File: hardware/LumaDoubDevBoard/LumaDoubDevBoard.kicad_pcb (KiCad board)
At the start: 4 copper layers, 99.5 x 99.5 mm, 188 parts, among them IC1 TPS2116DRLR, IC2 TPS62A01ADRLR, J2 217179-0001, J3 Conn_01x02_Pin, J4 Conn_01x08, J5 Conn_01x06, J6 Conn_01x08, J7 Conn_02x12_Odd_Even, P1 VGA_Male, P2 VGA_Male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

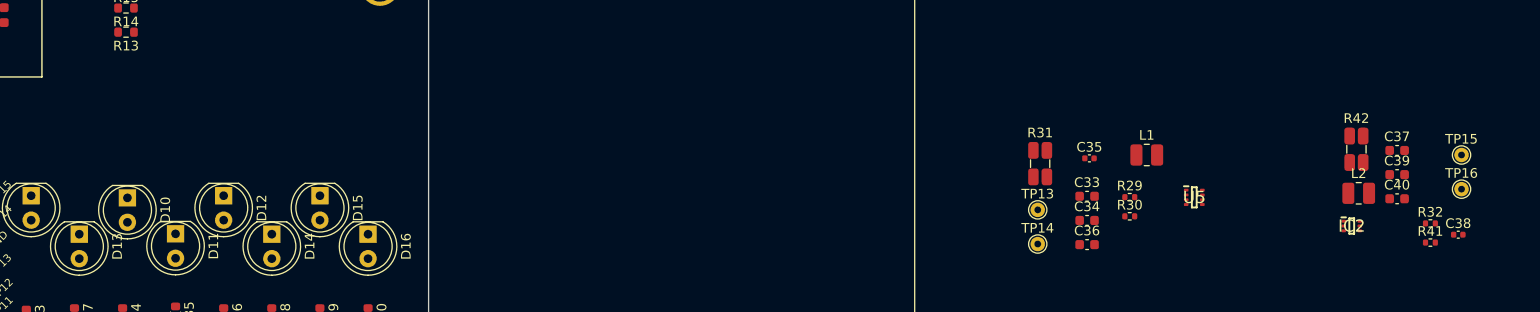
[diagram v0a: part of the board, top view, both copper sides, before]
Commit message: buck converter routing
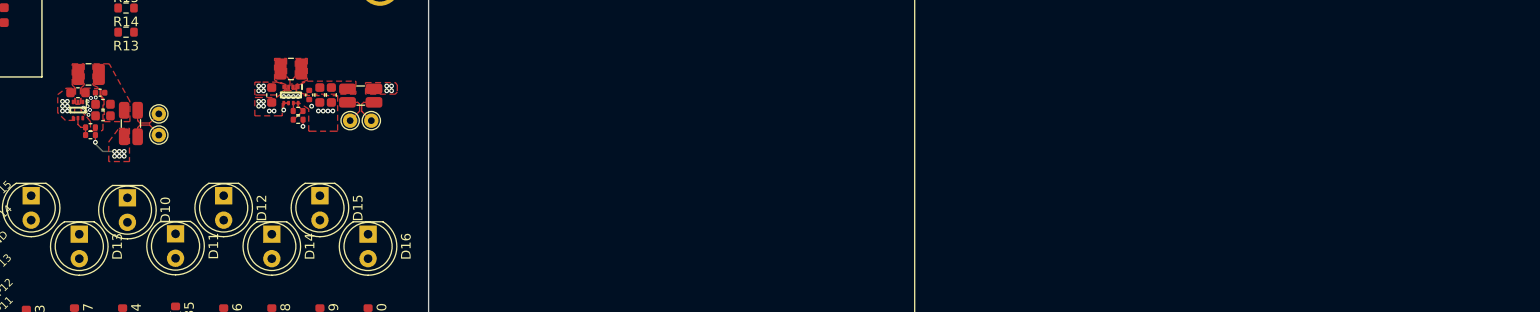
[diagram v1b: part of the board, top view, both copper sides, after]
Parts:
- moved C38 141.9 mm to (139.7, 85.5), turned to 180 degrees
- moved R41 139.7 mm to (138.7, 89.1)
- moved R32 139.5 mm to (138.7, 89.9), turned to 180 degrees
- moved C37 137.2 mm to (137.4, 85.5)
- moved TP16 135.5 mm to (145.8, 89.9)
- moved TP15 135.4 mm to (145.8, 87.7)
- moved C40 134.8 mm to (140.0, 86.7), turned to 180 degrees
- moved C39 134.6 mm to (140.0, 87.9), turned to 180 degrees
- moved IC2 132.9 mm to (137.4, 87.3), turned to -90 degrees
- moved L2 132.5 mm to (138.5, 83.6)
- moved R42 127.3 mm to (142.9, 88.7)
- moved U5 94.4 mm to (159.6, 85.7), turned to -90 degrees
- moved L1 89.4 mm to (159.6, 83.0)
- moved R30 87.1 mm to (160.3, 87.4), turned to 180 degrees
- moved R29 86.8 mm to (160.3, 88.3), turned to 180 degrees
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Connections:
- net DEBUG POWER renamed VMUX
- R42 pad 1: +1V89 -> Net-(C38-Pad1)
- R42 pad 4: Net-(C38-Pad1) -> +1V89
- TP15 pad 1: Net-(R42-Pad3) -> Net-(R42-Pad2)
- TP16 pad 1: Net-(R42-Pad2) -> Net-(R42-Pad3)
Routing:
- net Net-(R42-Pad2): track 0.00 -> 3.77 mm
- net Net-(R42-Pad3): track 0.00 -> 3.74 mm
- net Net-(R31-Pad2): track 0.00 -> 3.49 mm
- net Net-(R31-Pad3): track 0.00 -> 3.45 mm
- net +1V89: track 0.00 -> 3.35 mm, vias 0 -> 7
- net Net-(U5-FB): track 0.00 -> 2.43 mm
- net Net-(IC2-FB): track 0.00 -> 2.38 mm
- net VMUX: track 0.00 -> 1.22 mm, vias 0 -> 11
- net GND: track 13.1 -> 13.9 mm, vias 0 -> 23
- net +3V3: track 6.47 -> 7.17 mm, vias 0 -> 5
- added copper zone on F.Cu, net +1V89
- added copper zone on F.Cu, net +3V3
- added copper zone on F.Cu, net GND
- added copper zone on F.Cu, net Net-(C38-Pad1)
- added copper zone on F.Cu, net Net-(IC2-SW)
- added copper zone on F.Cu, net Net-(U5-LX1)
- added copper zone on F.Cu, net Net-(U5-LX2)
- added copper zone on F.Cu, net Net-(U5-VOUT)
- added copper zone on F.Cu, net VMUX
